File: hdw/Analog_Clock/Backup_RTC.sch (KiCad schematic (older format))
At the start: 16 parts, among them U1201 DS3231MZ, U1202 TLV6700

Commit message: more PCB grouping
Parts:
- U1202: footprint TO_SOT_Packages_SMD:TSOT-23-6 -> TO_SOT_Packages_SMD:SOT-23-6
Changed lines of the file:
@@
 F 0 "U1202" H 5630 4370 50  0000 C CNN
 F 1 "TLV6700" H 5330 4870 50  0000 C CNN
-F 2 "TO_SOT_Packages_SMD:TSOT-23-6" H 5330 5470 60  0001 C CNN
+F 2 "TO_SOT_Packages_SMD:SOT-23-6" H 5330 5470 60  0001 C CNN
 F 3 "http://www.ti.com/lit/ds/symlink/tlv6700.pdf" H 5330 4870 60  0001 C CNN
 F 4 "296-51696-1-ND" H 5330 4870 50  0001 C CNN "Digi-Key PN"

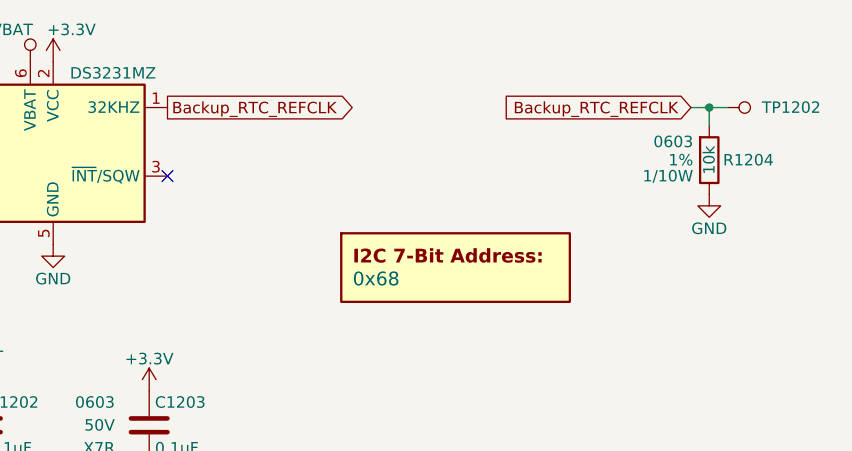
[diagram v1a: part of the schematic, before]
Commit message: Arranged more components on PCB
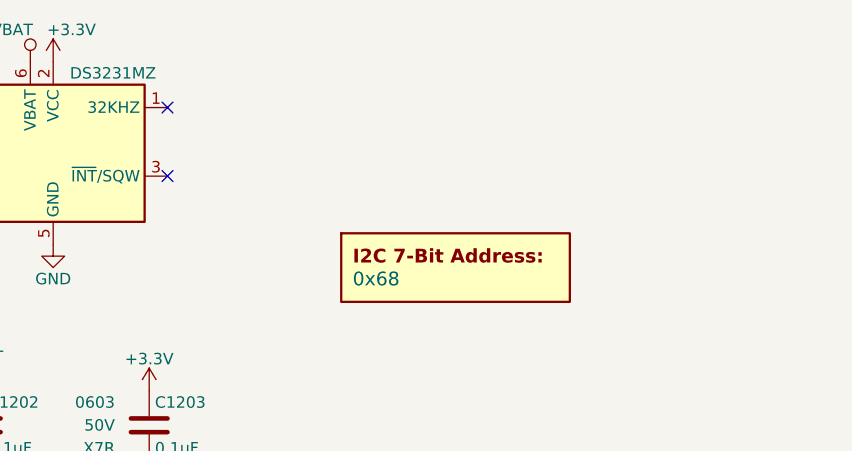
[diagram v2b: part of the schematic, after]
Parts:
- removed R1204: 10k, Resistors_SMD:R_0603, symbol Custom_Library:R_Custom
- removed TP1202: TP, Custom Footprints Library:Test_Point, symbol Custom_Library:TP
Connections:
- net Backup_RTC_REFCLK: no longer names the net of U1201.1 (32KHZ)
- no-connect marks 5 -> 6
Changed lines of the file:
@@
 	1    0    0    -1
 $EndComp
-Text GLabel 7840 1800 0    50   Input ~ 0
-Backup_RTC_REFCLK
-$Comp
-L Custom_Library:R_Custom R?
-U 1 1 5F3530B0
-P 7920 2030
-AR Path="/5BAAE1F3/5F3530B0" Ref="R?"  Part="1"
-AR Path="/5BAAE1DC/5F3530B0" Ref="R?"  Part="1"
-AR Path="/5BAAE16C/5F3530B0" Ref="R?"  Part="1"
-AR Path="/5BB844FD/5F3530B0" Ref="R?"  Part="1"
-AR Path="/5BF346B3/5F3530B0" Ref="R?"  Part="1"
-AR Path="/5CAD2D97/5F3530B0" Ref="R?"  Part="1"
-AR Path="/5CB7A8BC/5F3530B0" Ref="R?"  Part="1"
-AR Path="/5E01BCC3/5F3530B0" Ref="R?"  Part="1"
-AR Path="/5E697952/5F3530B0" Ref="R?"  Part="1"
-AR Path="/5EAE2F15/5F3530B0" Ref="R?"  Part="1"
-AR Path="/5E939EDE/5F3530B0" Ref="R?"  Part="1"
-AR Path="/5E939EED/5F3530B0" Ref="R1204"  Part="1"
-F 0 "R1204" H 7860 2030 50  0000 R CNN
-F 1 "10k" V 7920 2030 50  0000 C CNN
-F 2 "Resistors_SMD:R_0603" H 7920 2030 50  0001 C CNN
-F 3 "" H 7920 2030 50  0001 C CNN
-F 4 "0603" H 7990 2110 50  0000 L CNN "display_footprint"
-F 5 "1%" H 7990 2030 50  0000 L CNN "Tolerance"
-F 6 "1/10W" H 7990 1960 50  0000 L CNN "Wattage"
-F 7 "YAG2321CT-ND" H 7920 2030 50  0001 C CNN "Digi-Key PN"
-	1    7920 2030
-	-1   0    0    -1
-$EndComp
-$Comp
-L power:GND #PWR?
-U 1 1 5F3530B6
-P 7920 2180
-AR Path="/5E939EDE/5F3530B6" Ref="#PWR?"  Part="1"
-AR Path="/5E939EED/5F3530B6" Ref="#PWR01222"  Part="1"
-F 0 "#PWR01222" H 7920 1930 50  0001 C CNN
-F 1 "GND" H 7920 2030 50  0000 C CNN
-F 2 "" H 7920 2180 50  0001 C CNN
-F 3 "" H 7920 2180 50  0001 C CNN
-	1    7920 2180
-	1    0    0    -1
-$EndComp
-Wire Wire Line
-	7920 1880 7920 1800
-Wire Wire Line
-	7920 1800 7840 1800
-$Comp
-L Custom_Library:TP TP?
-U 1 1 5F3530BE
-P 8000 1800
-AR Path="/5C1D5CD8/5F3530BE" Ref="TP?"  Part="1"
-AR Path="/5C1D5C9E/5F3530BE" Ref="TP?"  Part="1"
-AR Path="/5CB6F1ED/5F3530BE" Ref="TP?"  Part="1"
-AR Path="/5E939CFF/5F3530BE" Ref="TP?"  Part="1"
-AR Path="/5E9E0E87/5F3530BE" Ref="TP?"  Part="1"
-AR Path="/5EAE2D66/5F3530BE" Ref="TP?"  Part="1"
-AR Path="/5EAE2F15/5F3530BE" Ref="TP?"  Part="1"
-AR Path="/5E939EDE/5F3530BE" Ref="TP?"  Part="1"
-AR Path="/5E939EED/5F3530BE" Ref="TP1202"  Part="1"
-F 0 "TP1202" V 8000 1950 50  0000 L CNN
-F 1 "TP" H 8000 1950 50  0001 C CNN
-F 2 "Custom Footprints Library:Test_Point" H 8000 1800 60  0001 C CNN
-F 3 "" H 8000 1800 60  0000 C CNN
-	1    8000 1800
-	0    1    1    0
-$EndComp
-Wire Wire Line
-	8000 1800 7920 1800
-Connection ~ 7920 1800
-Text GLabel 5550 1800 2    50   Output ~ 0
-Backup_RTC_REFCLK
 $Comp
 L Custom_Library:C_Custom C1204
@@
 	3300 4620 4130 4620
 Connection ~ 3300 4620
+NoConn ~ 5550 1800
 $EndSCHEMATC
